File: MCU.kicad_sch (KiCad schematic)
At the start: 21 parts, among them U1 NRF52810-QCAA-E-R7, Y1 32.768kHz, Y2 32MHz

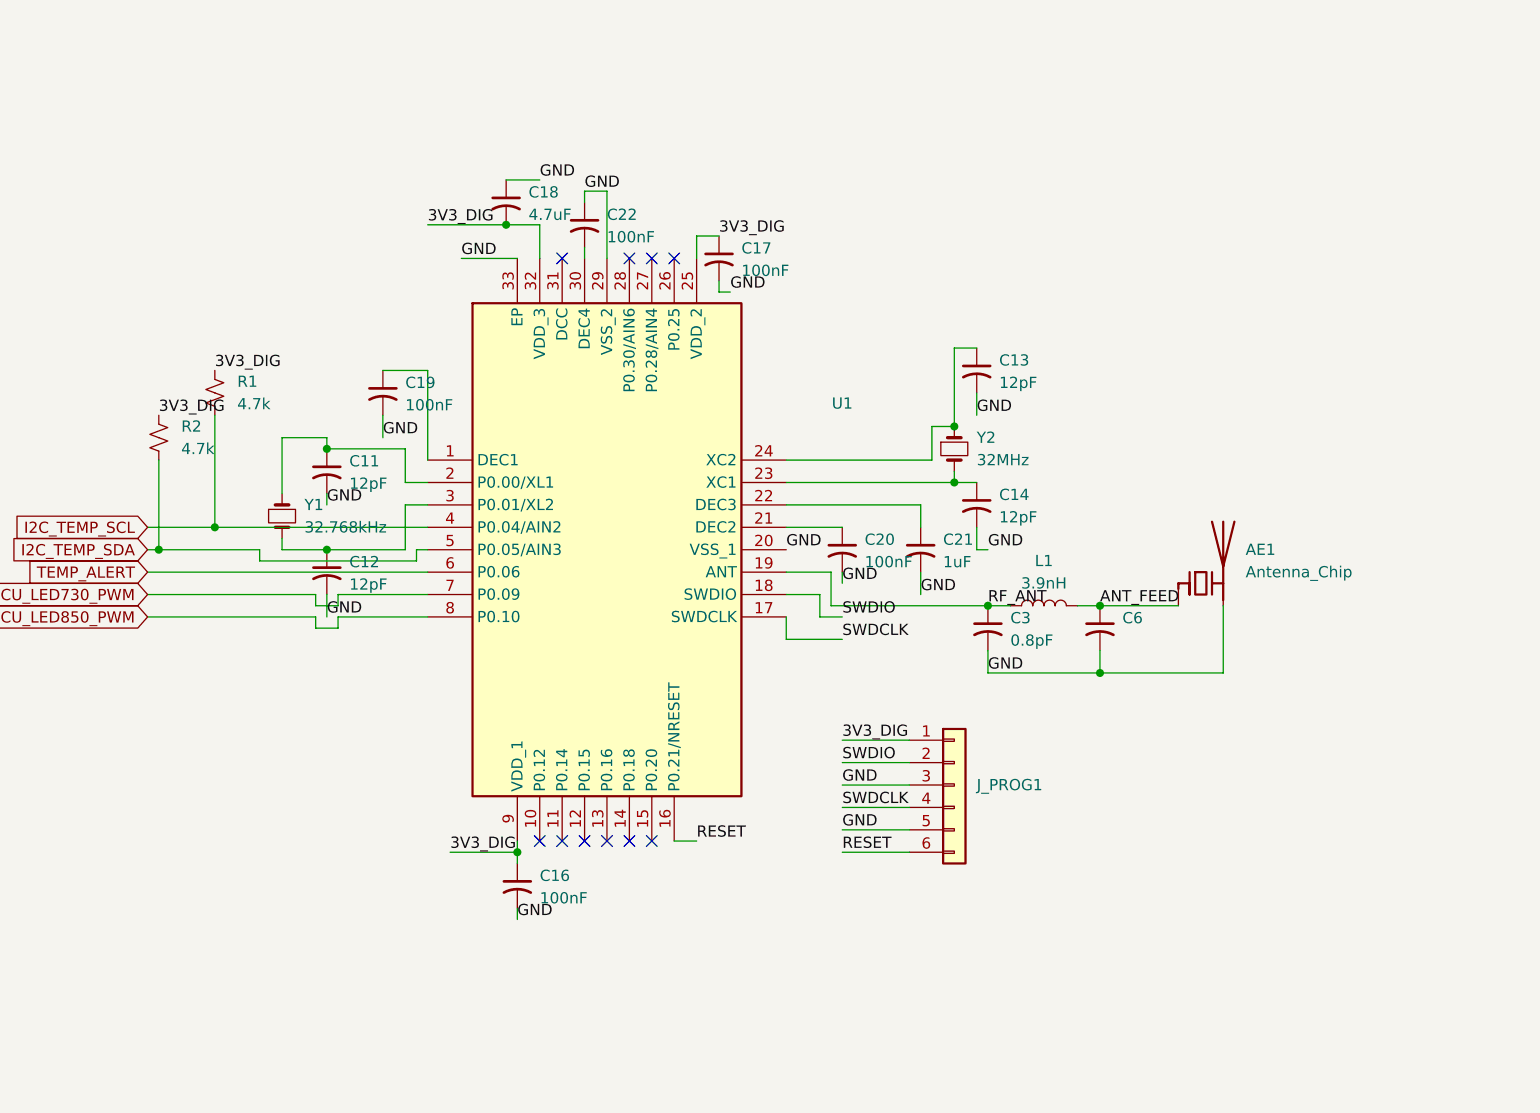
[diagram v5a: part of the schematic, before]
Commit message: replace mcu with module due to antenna tuning compexity
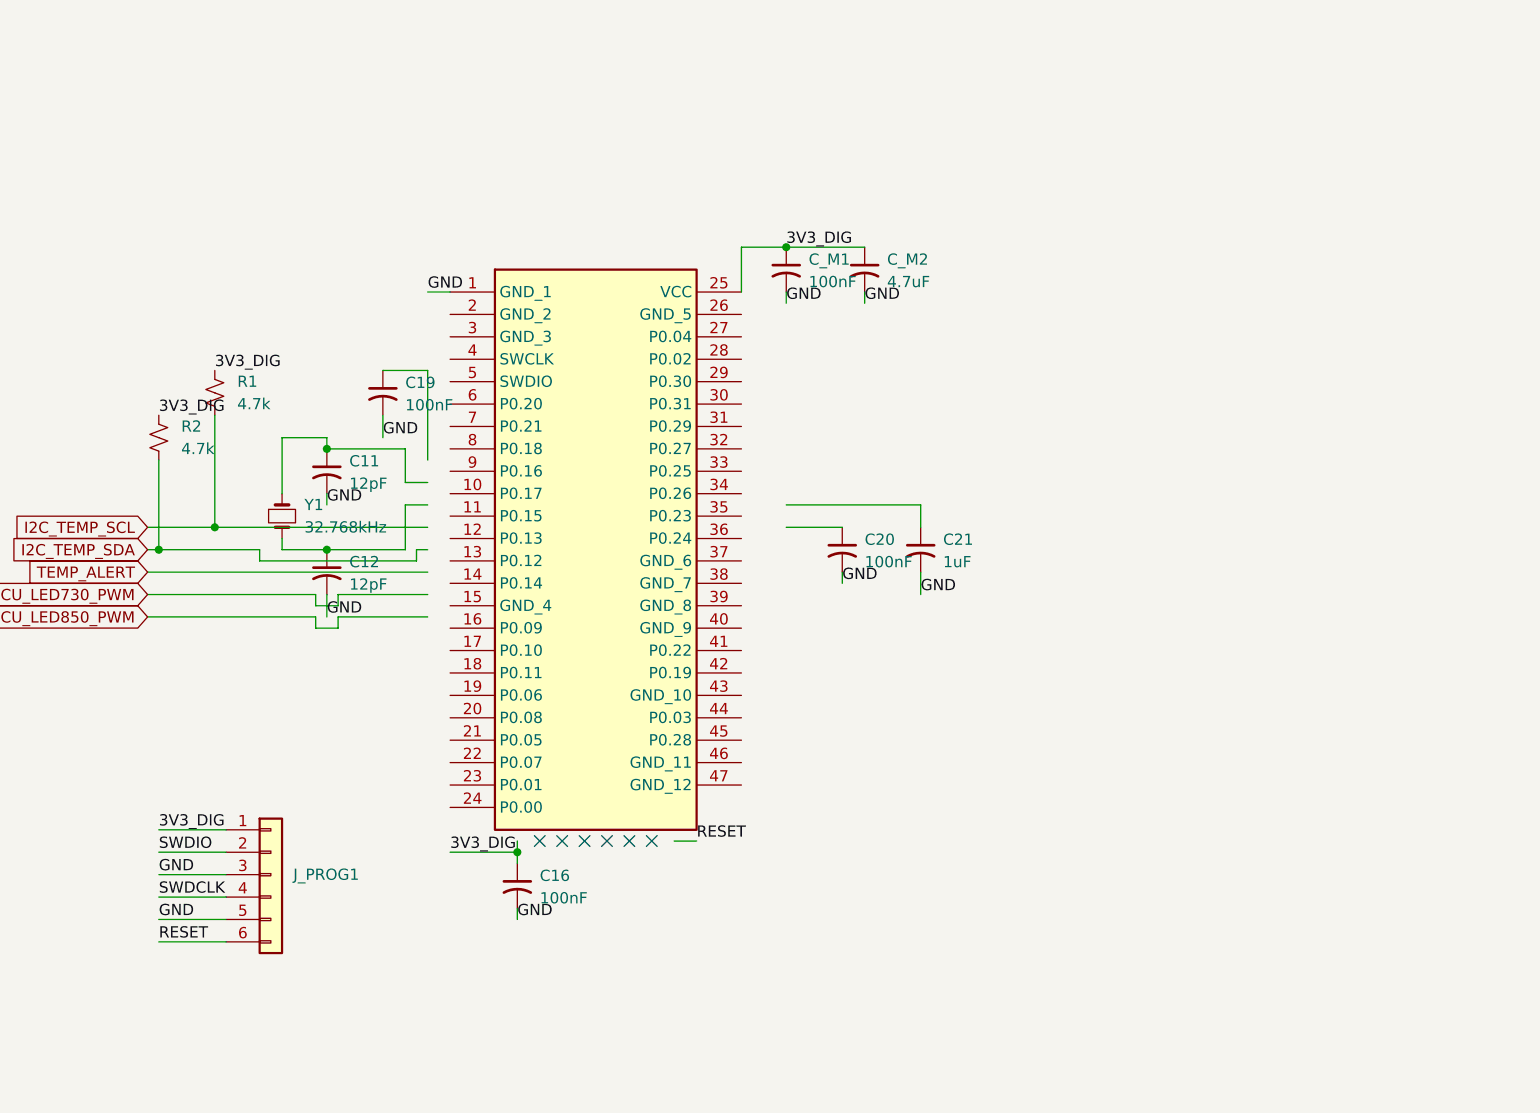
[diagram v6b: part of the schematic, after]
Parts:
- removed AE1: Antenna_Chip, symbol Device:Antenna_Chip
- removed C13, C14: 12pF, symbol Device:C_Small_US
- removed C22: 100nF, symbol Device:C_Small_US
- removed C3: 0.8pF, symbol Device:C_Small_US
- removed C6: Not mounted, symbol Device:C_Small_US
- removed L1: 3.9nH, symbol Device:L
- removed U1: NRF52810-QCAA-E-R7, NRF52810-QCAA-E-R7:QFN50P500X500X90-33N, symbol NRF52810-QCAA-E-R7:NRF52810-QCAA-E-R7
- removed Y2: 32MHz, symbol Device:Crystal_Small
- added U1: BMD-350-A-R, BMD-350, symbol BMD-350-A-R:BMD-350-A-R
- renumbered C17 to C_M1, C18 to C_M2
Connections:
- net 3V3_DIG: now also C_M2.1, U1.25 (VCC); no longer C_M2.2
- net GND: now also C_M2.2, U1.1 (GND_1); no longer C_M2.1
- no-connect marks 10 -> 6
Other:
- moved on the sheet: C_M1, C_M2, J_PROG1

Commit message: power
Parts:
- removed C11, C12: 12pF, symbol Device:C_Small_US
- removed C16, C19, C20: 100nF, symbol Device:C_Small_US
- removed C21: 1uF, symbol Device:C_Small_US
- removed Y1: 32.768kHz, symbol Device:Crystal_Small
- U1: footprint BMD-350 -> BMD-350-A-R:BMD-350
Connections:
- net GND: now also U1.15 (GND_4), U1.2 (GND_2), U1.26 (GND_5), U1.3 (GND_3), U1.37 (GND_6), U1.38 (GND_7), U1.39 (GND_8), U1.40 (GND_9), U1.43 (GND_10), U1.46 (GND_11), U1.47 (GND_12)
- net I2C_TEMP_SCL: now also U1.20 (P0.08)
- net I2C_TEMP_SDA: now also U1.18 (P0.11)
- net RESET: now also U1.7 (P0.21)
- net SWDCLK: now also U1.4 (SWCLK)
- net SWDIO: now also U1.5 (SWDIO)
- net TEMP_ALERT: now also U1.19 (P0.06)
- net PWM_730: now reaches U1.12 (P0.13)
- net PWM_850: now reaches U1.14 (P0.14)
- no-connect marks 6 -> 26
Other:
- added sheet 03_LED_DRIVERS_IR_OUTPUTS (03_LED_DRIVERS_IR_OUTPUTS.kicad_sch)
- moved on the sheet: R1, R2

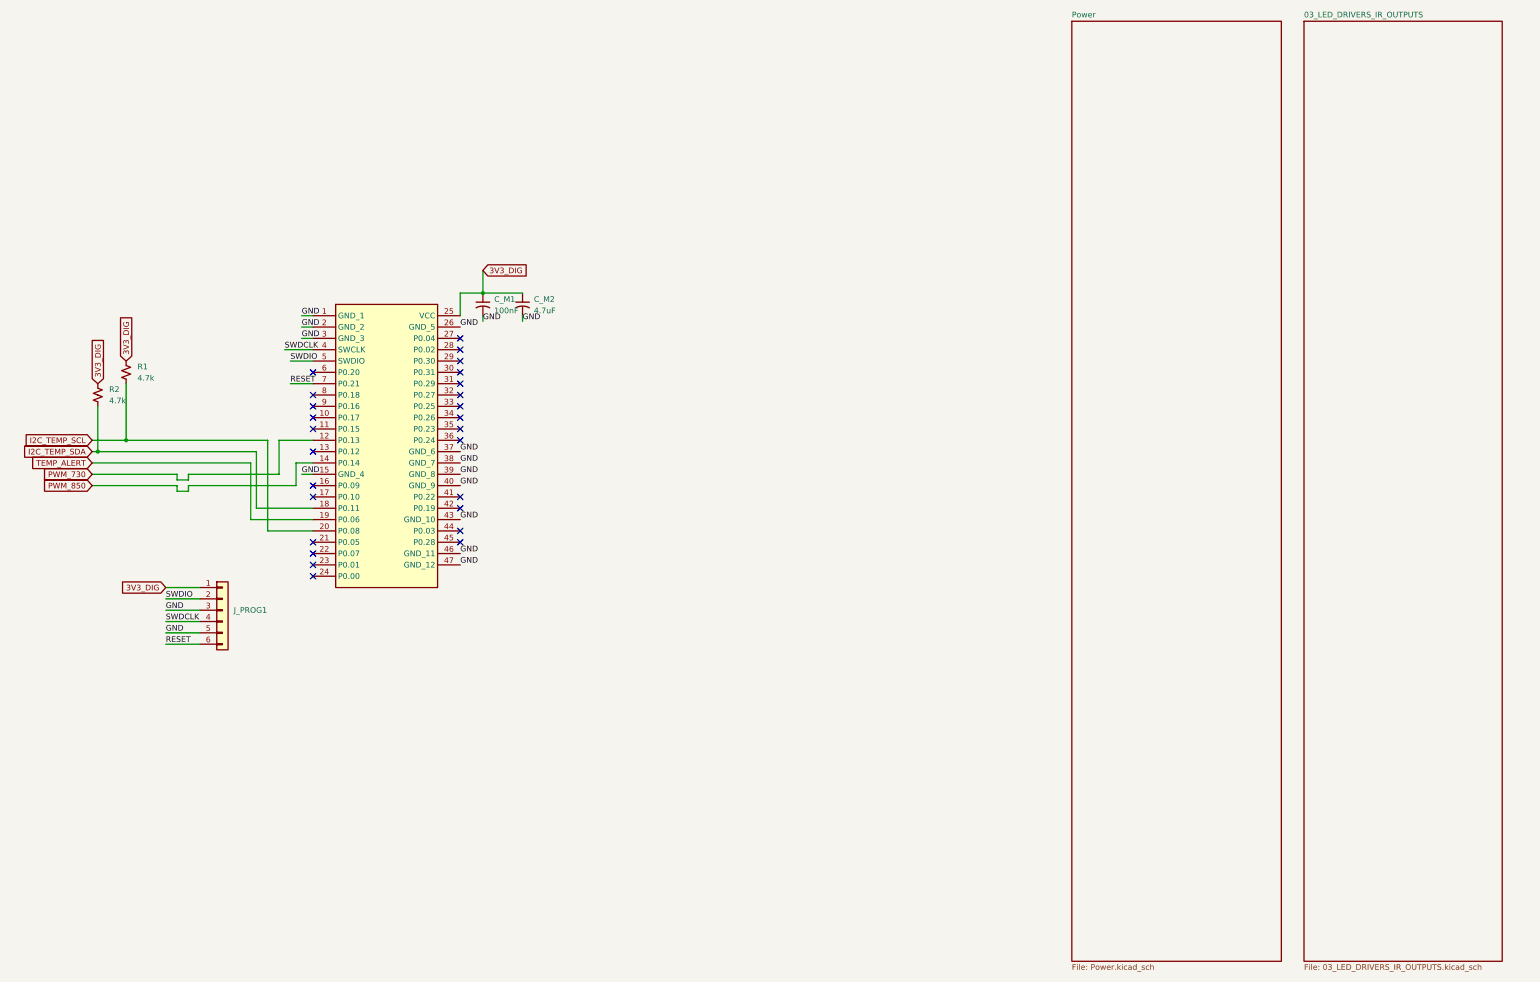
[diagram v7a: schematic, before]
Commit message: acc_power connector
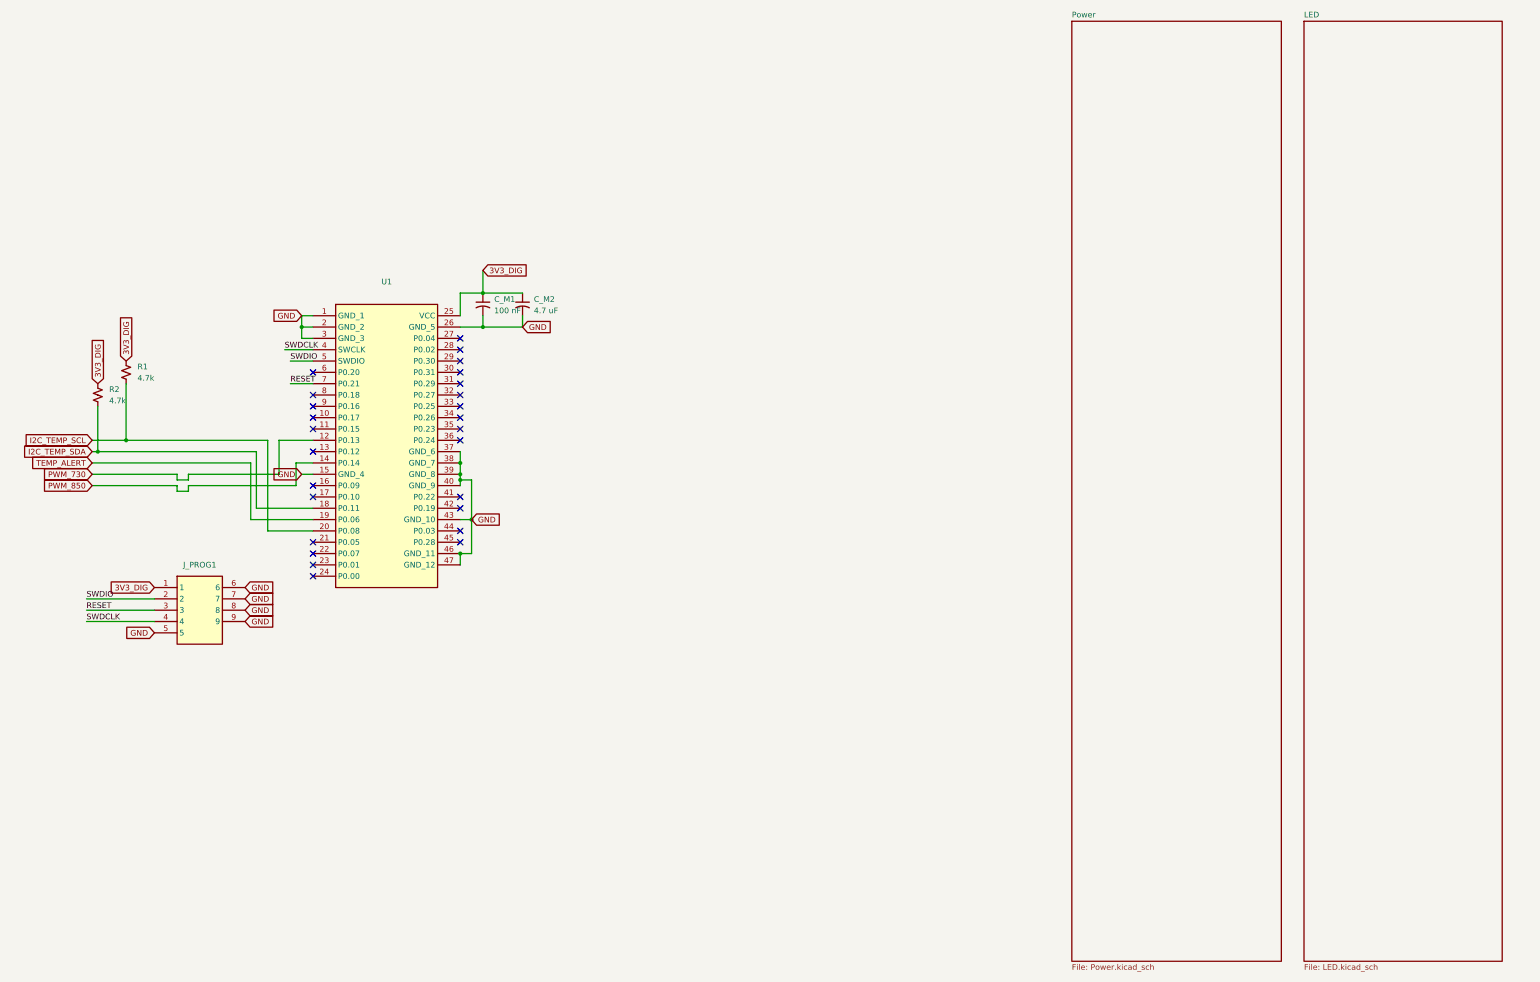
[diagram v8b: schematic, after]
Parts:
- C_M1: value 100nF -> 100 nF; footprint (none) -> LightFusion:C_0402_1005Metric; symbol Device:C_Small_US -> C_Small_US:C_Small_US
- C_M2: value 4.7uF -> 4.7 uF; footprint (none) -> LightFusion:C_0402_1005Metric; symbol Device:C_Small_US -> C_Small_US:C_Small_US
- J_PROG1: value TC2030-IDC-NL -> TC2030-IDC-FP; footprint Connector:Tag-Connect_TC2030-IDC-NL_2x03_P1.27mm_Vertical -> LightFusion:TC2030IDCFP; symbol Connector_Generic:Conn_01x06 -> TC2030-IDC-NL:TC2030-IDC-FP; Height (none) -> 18.669; MF (none) -> Tag Connect; Manufacturer_Name (none) -> Tag Connect; Manufacturer_Part_Number (none) -> TC2030-IDC-FP; PARTREV (none) -> A; STANDARD (none) -> Manufacturer Recommendations
- R1, R2: footprint (none) -> LightFusion:R_0402_1005Metric; symbol Device:R_Small_US -> R_Small_US:R_Small_US
- U1: footprint BMD-350-A-R:BMD-350 -> LightFusion:BMD-350
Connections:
- net GND: now also J_PROG1.6, J_PROG1.7, J_PROG1.8, J_PROG1.9; no longer J_PROG1.3 (Pin_3)
- net RESET: now also J_PROG1.3; no longer J_PROG1.6 (Pin_6)
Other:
- sheet 03_LED_DRIVERS_IR_OUTPUTS renamed LED
- sheet LED: file 03_LED_DRIVERS_IR_OUTPUTS.kicad_sch -> LED.kicad_sch
